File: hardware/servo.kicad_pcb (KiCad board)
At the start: 2 copper layers, 43 x 44 mm, 37 parts, among them J1 servo, J2 Jack-DC, J3 swd, Q2 DMT64M8LSS, SW1 restart, SW2 buzzer, U1 AOZ1284PI, U3 STM32G030F6Px, U4 LDI1117-3.3U-DIO

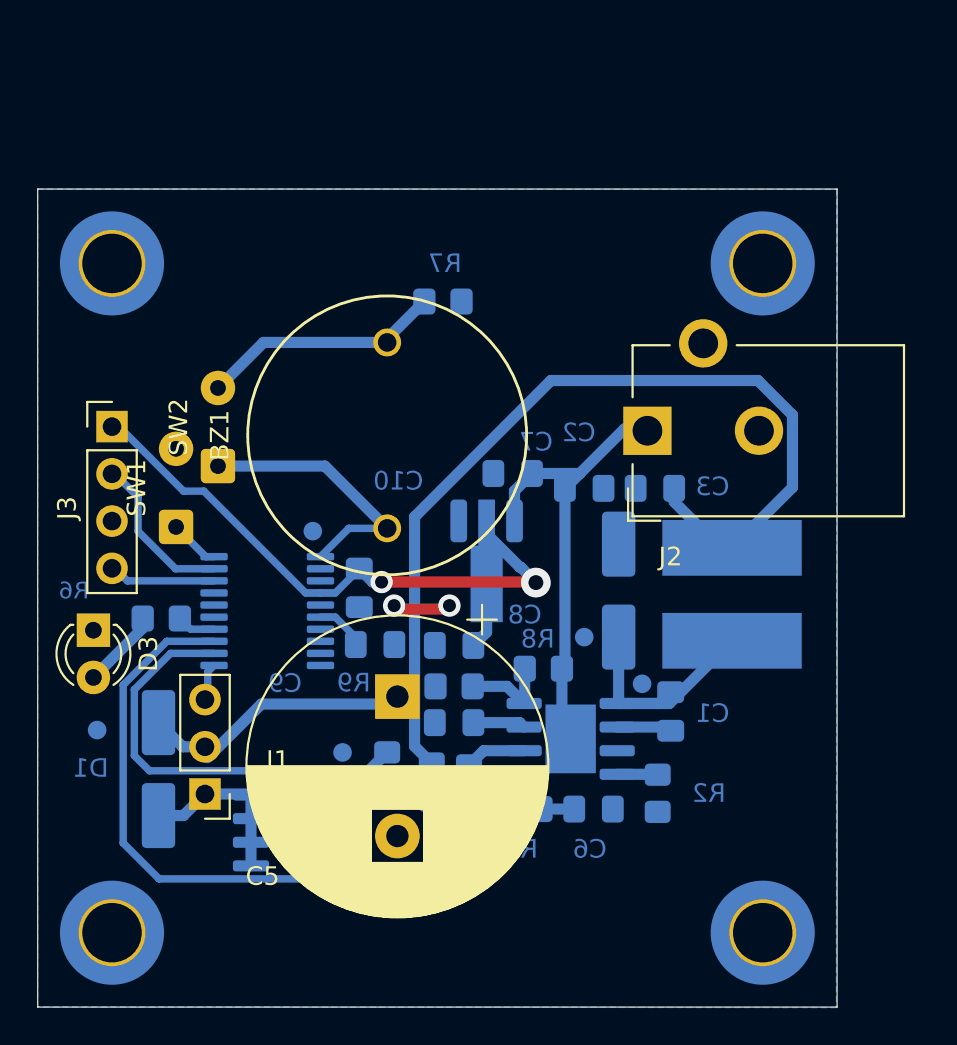
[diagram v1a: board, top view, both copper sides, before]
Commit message: Fix getting stuck in bootloader, false overcurrent triggers
HARDWARE: add BOOT0 pulldown, reduce buzzer resistance for more volume, add drill hole for AOZ1284 footprint EPAD
SOFTWARE: add ADC delay for motor inrush, add software lowpass filtering to overcurrent protection
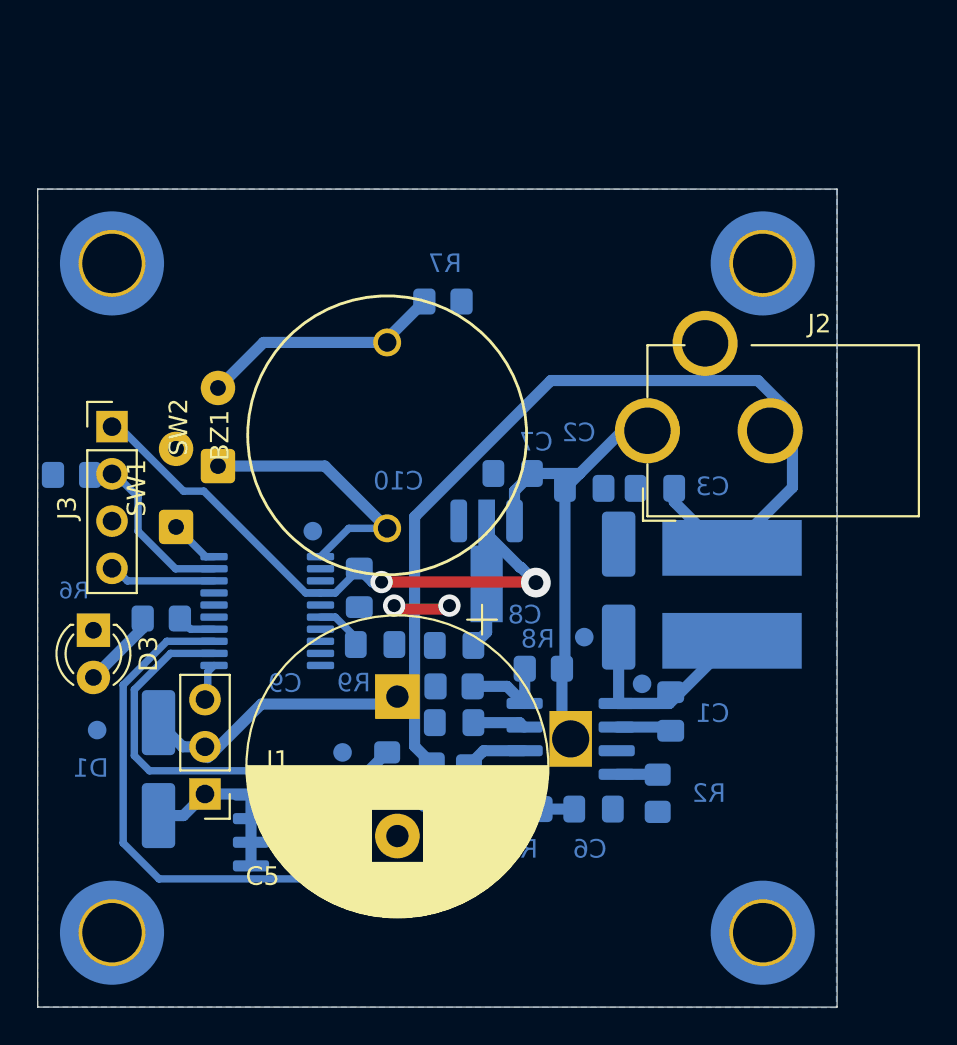
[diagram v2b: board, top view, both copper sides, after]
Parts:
- added R10: 10k, Resistor_SMD:R_0805_2012Metric_Pad1.20x1.40mm_HandSolder, B.Cu at (1.82, 15.4)
- J2: footprint Connector_BarrelJack:BarrelJack_CUI_PJ-102AH_Horizontal -> Connector_BarrelJack:BarrelJack_diy
- R6: value 1.3k -> 150
- R7: value 51k -> 300
- U1: footprint Package_SO:SOIC-8-1EP_3.9x4.9mm_P1.27mm_EP2.71x3.7mm -> Package_SO:SOIC-8-1EP_3.9x4.9mm_P1.27mm_EP2.29x3mm_diy
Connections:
- net /mosfet renamed /fet

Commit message: Hardware and software fixes, reorganize
Recalculate compensation for 4.7mF, increase ADC delay, improve code readability, match compensation annotation in schematic to datasheet
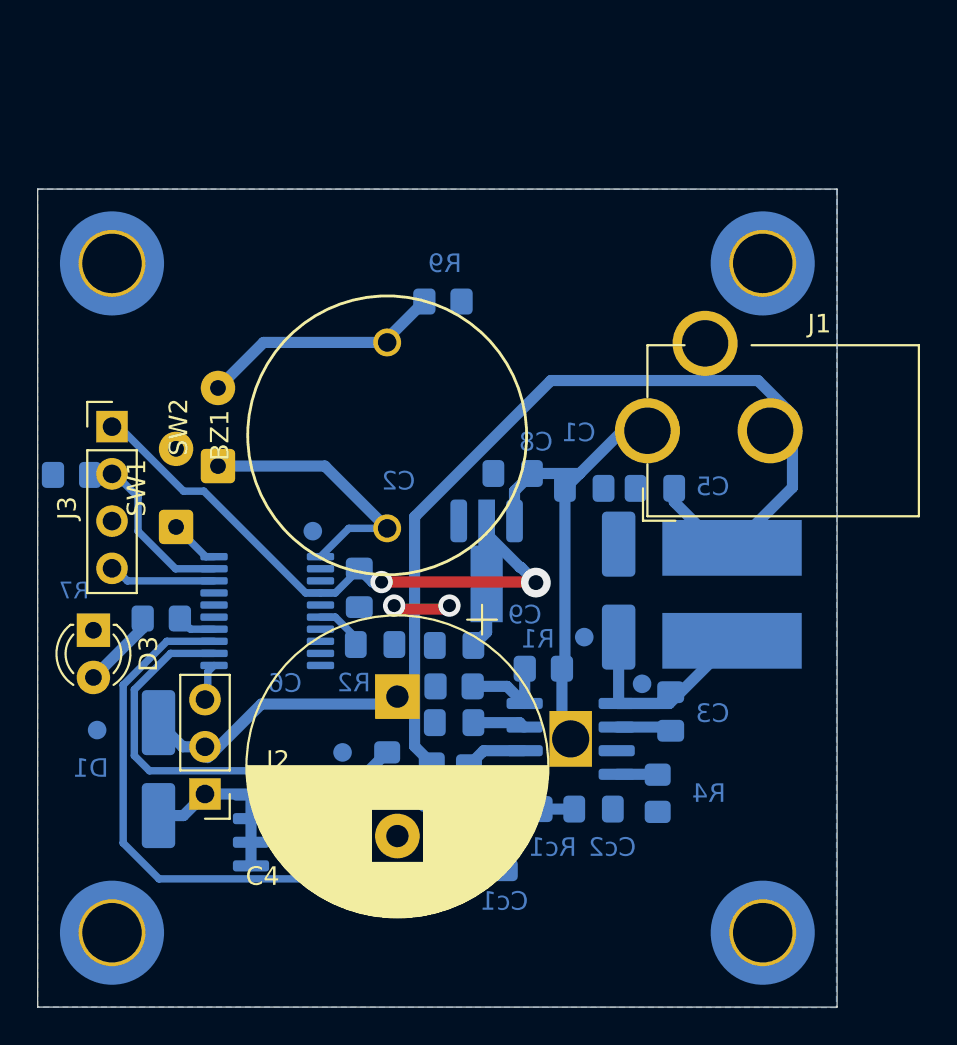
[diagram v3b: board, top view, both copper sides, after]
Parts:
- added Cc1: 1.5n, Capacitor_SMD:C_0805_2012Metric_Pad1.18x1.45mm_HandSolder, B.Cu at (25.1, 35.6)
- renumbered C2 to C1, C10 to C2, C1 to C3, C5 to C4, C3 to C5, C9 to C6, C4 to C7, C7 to C8, C8 to C9, C6 to Cc2, J2 to J1, J1 to J2, Q2 to Q1, R8 to R1, R9 to R2, R1 to R3, R2 to R4, R3 to R5, R5 to R6, R6 to R7, R10 to R8, R7 to R9, R4 to Rc1, U4 to U2

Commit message: Add connector for LEDs, finished PCB picture
Add connector for LED module, finished PCB picture, edit schematic for readability
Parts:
- added J4: LED, Connector_Phoenix_MSTB:PhoenixContact_MSTBA_2,5_2-G-5,08_1x02_P5.08mm_Horizontal, F.Cu at (28.7, 2.00)
- Cc1: value 1.5n -> 150p
- Cc2: value 1.5n -> 6.8n
- J1: value Jack-DC -> 5.5x2.1
- Rc1: value 10k -> 1M
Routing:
- net +12V: track 25.0 -> 39.2 mm, vias 0 -> 2
